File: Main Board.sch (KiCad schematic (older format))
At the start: 0 parts

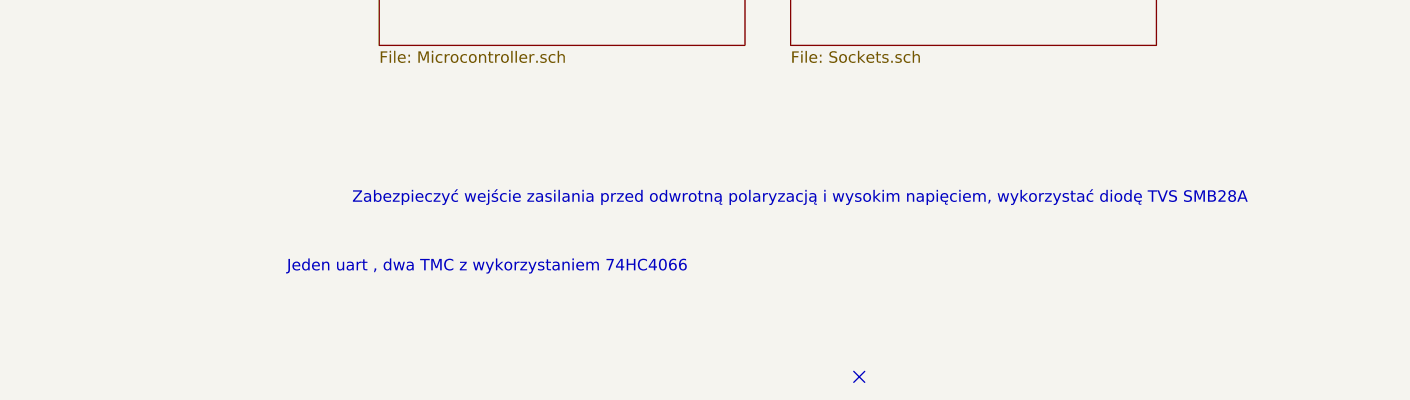
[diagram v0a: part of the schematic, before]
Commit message: Finished Power Managment
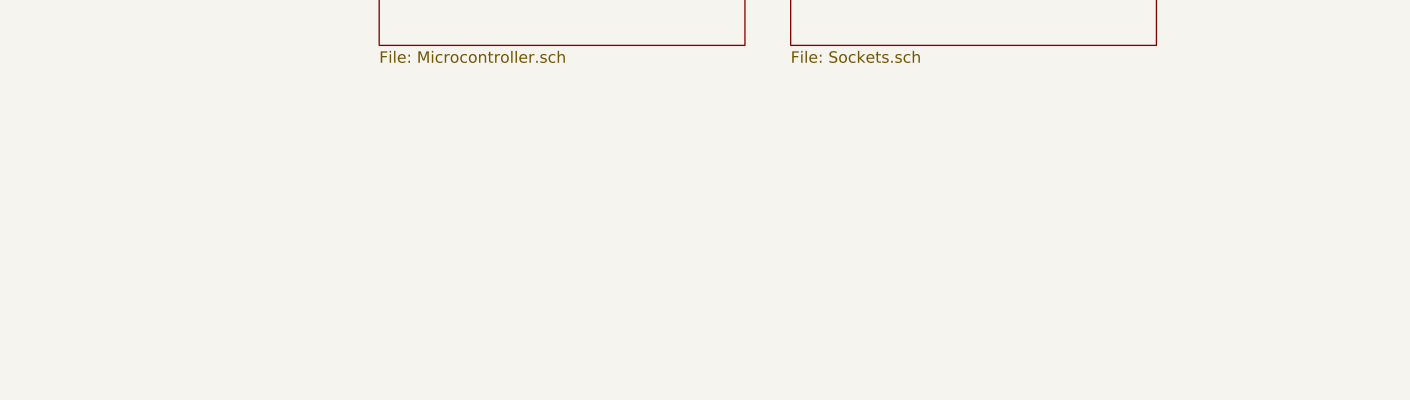
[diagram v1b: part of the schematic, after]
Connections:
- no-connect marks 1 -> 0
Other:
- note removed: "Jeden uart , dwa TMC z wykorzystaniem 74HC4066\n"
- note removed: "Zabezpieczyć wejście zasilania przed odwrotną polaryzacją i wysokim napięciem, wykorzystać diodę TVS SMB28A"
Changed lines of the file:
@@
 F1 "Sockets.sch" 50
 $EndSheet
-Text Notes 5550 3650 2    50   ~ 0
-Zabezpieczyć wejście zasilania przed odwrotną polaryzacją i wysokim napięciem, wykorzystać diodę TVS SMB28A
-NoConn ~ 3850 4400
-Text Notes 3100 3950 2    50   ~ 0
-Jeden uart , dwa TMC z wykorzystaniem 74HC4066\n
 $Sheet
 S 5400 800  1600 900

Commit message: Finished Emergency Circuit
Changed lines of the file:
@@
 $Descr A4 11693 8268
 encoding utf-8
-Sheet 1 6
+Sheet 1 9
 Title ""
 Date ""
@@
 F1 "Power.sch" 50
 $EndSheet
+$Sheet
+S 5400 2050 1600 900
+U 5E858220
+F0 "Sockets 2" 50
+F1 "Sockets 2.sch" 50
+$EndSheet
+$Sheet
+S 1750 3250 1600 900
+U 5E91D7CC
+F0 "Emergency" 50
+F1 "Emergency.sch" 50
+$EndSheet
+$Sheet
+S 3550 3250 1600 900
+U 5E91D96F
+F0 "HMI" 50
+F1 "HMI.sch" 50
+$EndSheet
 $EndSCHEMATC

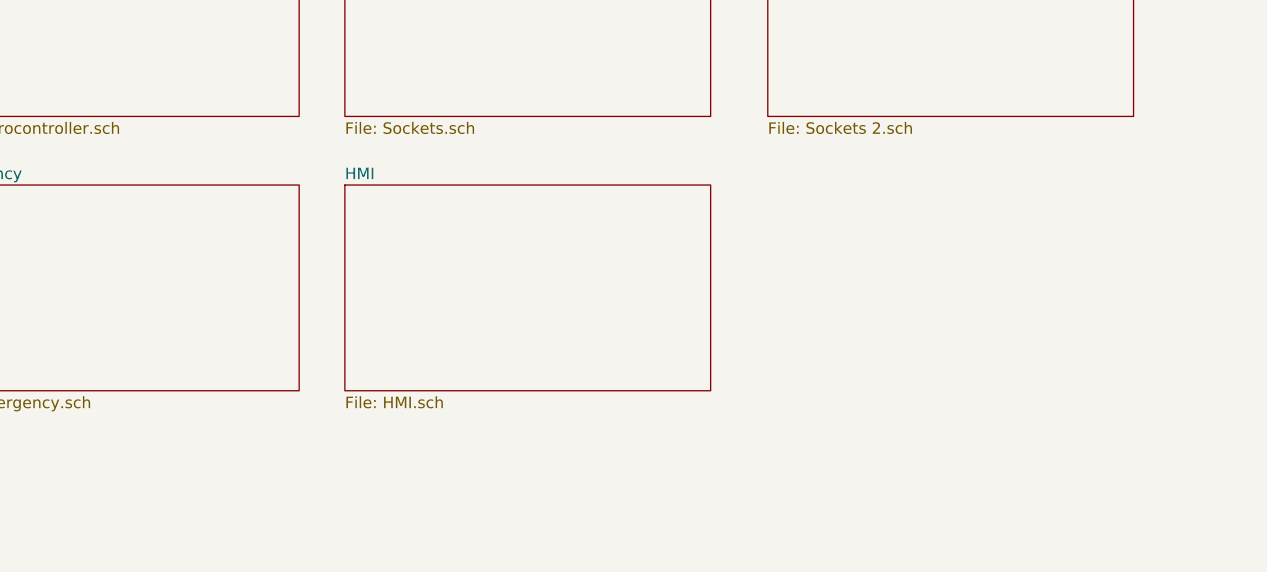
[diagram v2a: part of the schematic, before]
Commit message: Added Polyfuses and replace diodes
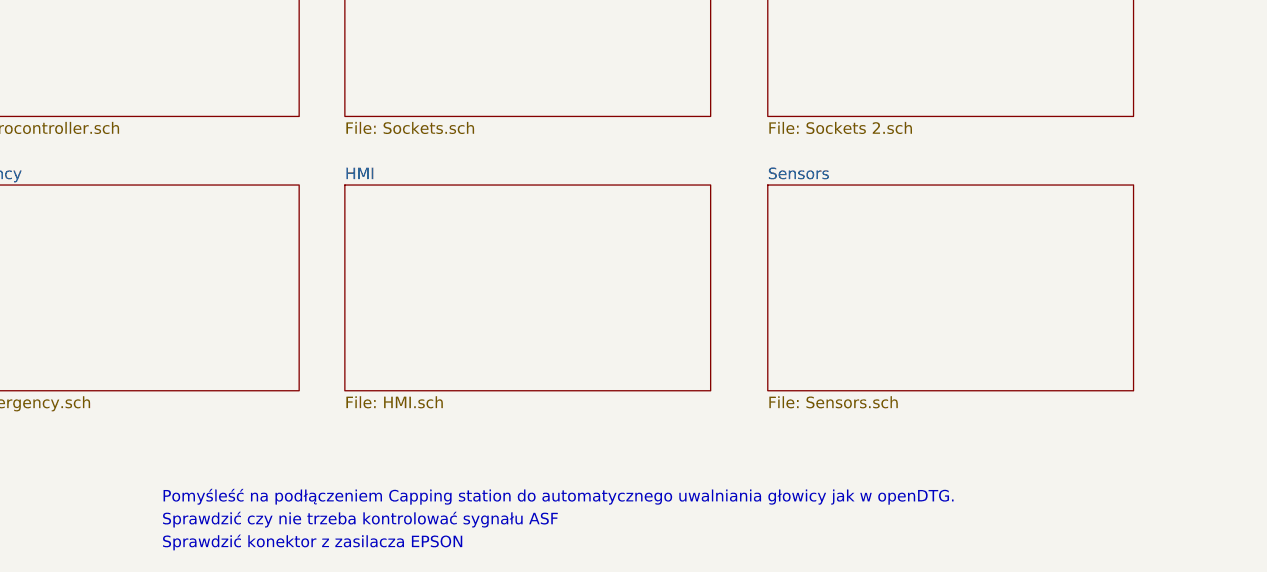
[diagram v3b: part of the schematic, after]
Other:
- note added: "Pomyśleść na podłączeniem Capping station do automatycznego uwalniania głowicy jak w openDTG."
- note added: "Sprawdzić czy nie trzeba kontrolować sygnału ASF"
- note added: "Sprawdzić konektor z zasilacza EPSON"
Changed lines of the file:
@@
 $Descr A4 11693 8268
 encoding utf-8
-Sheet 1 9
+Sheet 1 10
 Title ""
 Date ""
@@
 F1 "HMI.sch" 50
 $EndSheet
+$Sheet
+S 5400 3250 1600 900
+U 5E1B3A8F
+F0 "Sensors" 50
+F1 "Sensors.sch" 50
+$EndSheet
+Text Notes 2750 4650 0    50   ~ 0
+Pomyśleść na podłączeniem Capping station do automatycznego uwalniania głowicy jak w openDTG.
+Text Notes 2750 4750 0    50   ~ 0
+Sprawdzić czy nie trzeba kontrolować sygnału ASF
+Text Notes 2750 4850 0    50   ~ 0
+Sprawdzić konektor z zasilacza EPSON
 $EndSCHEMATC

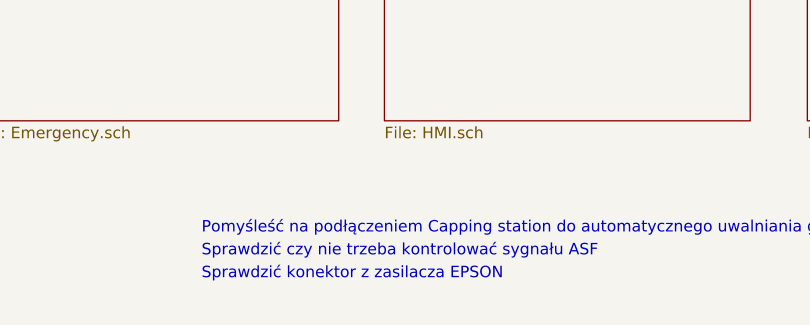
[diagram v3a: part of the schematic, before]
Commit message: Added USB B socket with ESD filter
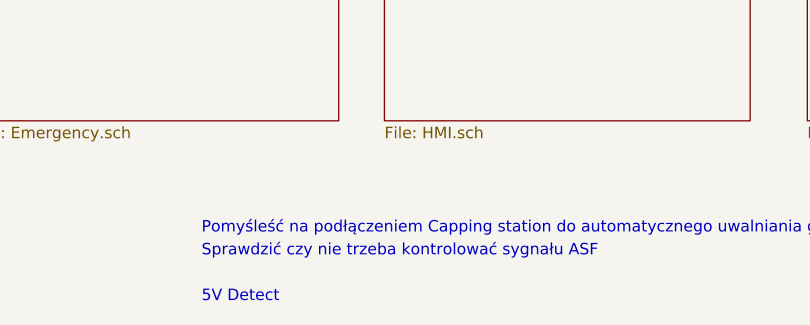
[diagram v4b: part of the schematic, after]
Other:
- note added: "5V Detect"
- note removed: "Sprawdzić konektor z zasilacza EPSON"
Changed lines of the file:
@@
 Text Notes 2750 4750 0    50   ~ 0
 Sprawdzić czy nie trzeba kontrolować sygnału ASF
-Text Notes 2750 4850 0    50   ~ 0
-Sprawdzić konektor z zasilacza EPSON
+Text Notes 2750 4950 0    50   ~ 0
+5V Detect
 $EndSCHEMATC

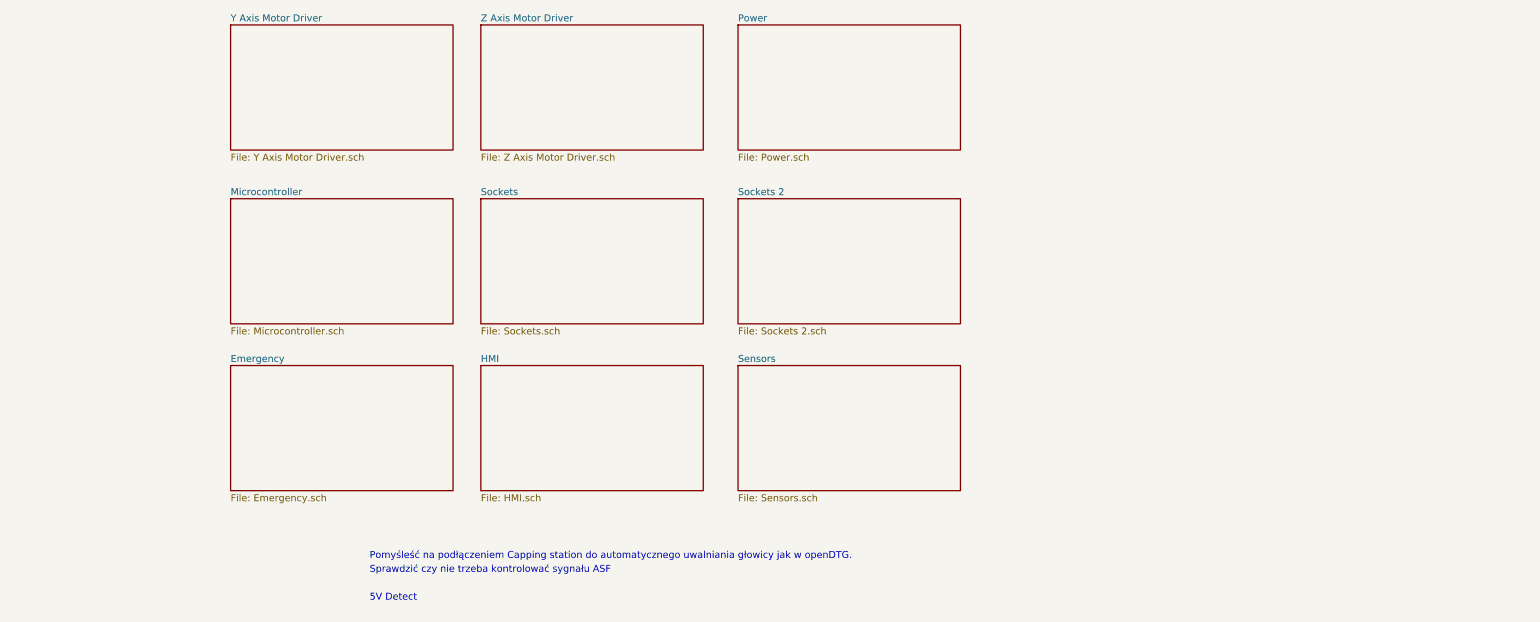
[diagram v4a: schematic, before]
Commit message: Numbering and finishing the schematic
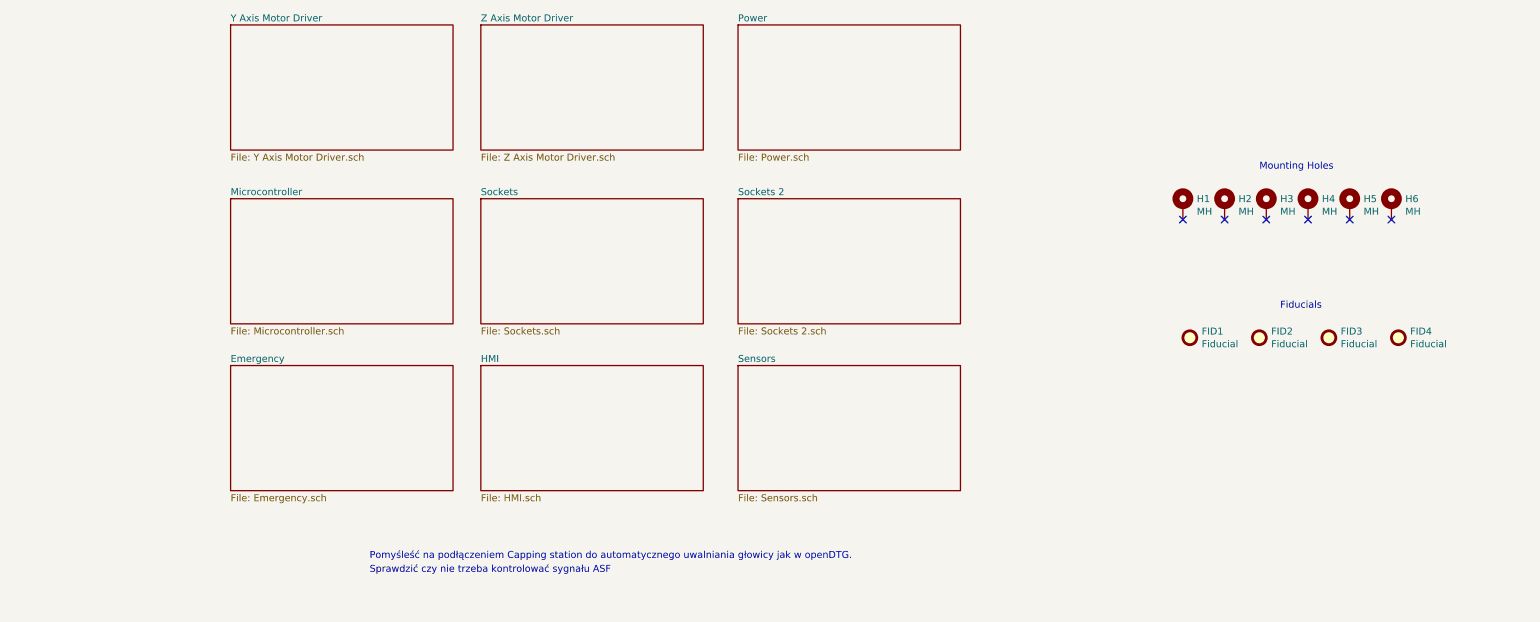
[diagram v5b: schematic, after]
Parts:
- added FID1, FID2, FID3, FID4: Fiducial, symbol Mechanical:Fiducial
- added H1, H2, H3, H4, H5, H6: MH, symbol Mechanical:MountingHole_Pad
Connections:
- no-connect marks 0 -> 6
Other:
- note added: "Fiducials"
- note added: "Mounting Holes"
- note removed: "5V Detect"
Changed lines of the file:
@@
 Text Notes 2750 4750 0    50   ~ 0
 Sprawdzić czy nie trzeba kontrolować sygnału ASF
-Text Notes 2750 4950 0    50   ~ 0
-5V Detect
+$Comp
+L Mechanical:MountingHole_Pad H1
+U 1 1 5E6920D8
+P 8600 2100
+F 0 "H1" H 8700 2149 50  0000 L CNN
+F 1 "MH" H 8700 2058 50  0000 L CNN
+F 2 "" H 8600 2100 50  0001 C CNN
+F 3 "~" H 8600 2100 50  0001 C CNN
+	1    8600 2100
+	1    0    0    -1
+$EndComp
+$Comp
+L Mechanical:MountingHole_Pad H2
+U 1 1 5E693034
+P 8900 2100
+F 0 "H2" H 9000 2149 50  0000 L CNN
+F 1 "MH" H 9000 2058 50  0000 L CNN
+F 2 "" H 8900 2100 50  0001 C CNN
+F 3 "~" H 8900 2100 50  0001 C CNN
+	1    8900 2100
+	1    0    0    -1
+$EndComp
+$Comp
+L Mechanical:MountingHole_Pad H3
+U 1 1 5E6931F2
+P 9200 2100
+F 0 "H3" H 9300 2149 50  0000 L CNN
+F 1 "MH" H 9300 2058 50  0000 L CNN
+F 2 "" H 9200 2100 50  0001 C CNN
+F 3 "~" H 9200 2100 50  0001 C CNN
+	1    9200 2100
+	1    0    0    -1
+$EndComp
+$Comp
+L Mechanical:MountingHole_Pad H4
+U 1 1 5E6933CD
+P 9500 2100
+F 0 "H4" H 9600 2149 50  0000 L CNN
+F 1 "MH" H 9600 2058 50  0000 L CNN
+F 2 "" H 9500 2100 50  0001 C CNN
+F 3 "~" H 9500 2100 50  0001 C CNN
+	1    9500 2100
+	1    0    0    -1
+$EndComp
+$Comp
+L Mechanical:MountingHole_Pad H5
+U 1 1 5E6935B4
+P 9800 2100
+F 0 "H5" H 9900 2149 50  0000 L CNN
+F 1 "MH" H 9900 2058 50  0000 L CNN
+F 2 "" H 9800 2100 50  0001 C CNN
+F 3 "~" H 9800 2100 50  0001 C CNN
+	1    9800 2100
+	1    0    0    -1
+$EndComp
+$Comp
+L Mechanical:MountingHole_Pad H6
+U 1 1 5E69378B
+P 10100 2100
+F 0 "H6" H 10200 2149 50  0000 L CNN
+F 1 "MH" H 10200 2058 50  0000 L CNN
+F 2 "" H 10100 2100 50  0001 C CNN
+F 3 "~" H 10100 2100 50  0001 C CNN
+	1    10100 2100
+	1    0    0    -1
+$EndComp
+NoConn ~ 8600 2200
+NoConn ~ 8900 2200
+NoConn ~ 9200 2200
+NoConn ~ 9500 2200
+NoConn ~ 9800 2200
+NoConn ~ 10100 2200
+$Comp
+L Mechanical:Fiducial FID1
+U 1 1 5E693F35
+P 8650 3050
+F 0 "FID1" H 8735 3096 50  0000 L CNN
+F 1 "Fiducial" H 8735 3005 50  0000 L CNN
+F 2 "" H 8650 3050 50  0001 C CNN
+F 3 "~" H 8650 3050 50  0001 C CNN
+	1    8650 3050
+	1    0    0    -1
+$EndComp
+$Comp
+L Mechanical:Fiducial FID2
+U 1 1 5E6942E3
+P 9150 3050
+F 0 "FID2" H 9235 3096 50  0000 L CNN
+F 1 "Fiducial" H 9235 3005 50  0000 L CNN
+F 2 "" H 9150 3050 50  0001 C CNN
+F 3 "~" H 9150 3050 50  0001 C CNN
+	1    9150 3050
+	1    0    0    -1
+$EndComp
+$Comp
+L Mechanical:Fiducial FID3
+U 1 1 5E694478
+P 9650 3050
+F 0 "FID3" H 9735 3096 50  0000 L CNN
+F 1 "Fiducial" H 9735 3005 50  0000 L CNN
+F 2 "" H 9650 3050 50  0001 C CNN
+F 3 "~" H 9650 3050 50  0001 C CNN
+	1    9650 3050
+	1    0    0    -1
+$EndComp
+$Comp
+L Mechanical:Fiducial FID4
+U 1 1 5E694686
+P 10150 3050
+F 0 "FID4" H 10235 3096 50  0000 L CNN
+F 1 "Fiducial" H 10235 3005 50  0000 L CNN
+F 2 "" H 10150 3050 50  0001 C CNN
+F 3 "~" H 10150 3050 50  0001 C CNN
+	1    10150 3050
+	1    0    0    -1
+$EndComp
+Text Notes 9150 1850 0    50   ~ 0
+Mounting Holes
+Text Notes 9300 2850 0    50   ~ 0
+Fiducials
 $EndSCHEMATC

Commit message: Shematic almost finished, BOM in KiCad 3/4 finished
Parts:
- FID1, FID2, FID3, FID4: footprint (none) -> Fiducial:Fiducial_1mm_Mask2mm
- H1, H2, H3, H4, H5, H6: footprint (none) -> MountingHole:MountingHole_3.5mm_Pad_Via
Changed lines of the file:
@@
 F 0 "H1" H 8700 2149 50  0000 L CNN
 F 1 "MH" H 8700 2058 50  0000 L CNN
-F 2 "" H 8600 2100 50  0001 C CNN
+F 2 "MountingHole:MountingHole_3.5mm_Pad_Via" H 8600 2100 50  0001 C CNN
 F 3 "~" H 8600 2100 50  0001 C CNN
 	1    8600 2100
@@
 F 0 "H2" H 9000 2149 50  0000 L CNN
 F 1 "MH" H 9000 2058 50  0000 L CNN
-F 2 "" H 8900 2100 50  0001 C CNN
+F 2 "MountingHole:MountingHole_3.5mm_Pad_Via" H 8900 2100 50  0001 C CNN
 F 3 "~" H 8900 2100 50  0001 C CNN
 	1    8900 2100
@@
 F 0 "H3" H 9300 2149 50  0000 L CNN
 F 1 "MH" H 9300 2058 50  0000 L CNN
-F 2 "" H 9200 2100 50  0001 C CNN
+F 2 "MountingHole:MountingHole_3.5mm_Pad_Via" H 9200 2100 50  0001 C CNN
 F 3 "~" H 9200 2100 50  0001 C CNN
 	1    9200 2100
@@
 F 0 "H4" H 9600 2149 50  0000 L CNN
 F 1 "MH" H 9600 2058 50  0000 L CNN
-F 2 "" H 9500 2100 50  0001 C CNN
+F 2 "MountingHole:MountingHole_3.5mm_Pad_Via" H 9500 2100 50  0001 C CNN
 F 3 "~" H 9500 2100 50  0001 C CNN
 	1    9500 2100
@@
 F 0 "H5" H 9900 2149 50  0000 L CNN
 F 1 "MH" H 9900 2058 50  0000 L CNN
-F 2 "" H 9800 2100 50  0001 C CNN
+F 2 "MountingHole:MountingHole_3.5mm_Pad_Via" H 9800 2100 50  0001 C CNN
 F 3 "~" H 9800 2100 50  0001 C CNN
 	1    9800 2100
@@
 F 0 "H6" H 10200 2149 50  0000 L CNN
 F 1 "MH" H 10200 2058 50  0000 L CNN
-F 2 "" H 10100 2100 50  0001 C CNN
+F 2 "MountingHole:MountingHole_3.5mm_Pad_Via" H 10100 2100 50  0001 C CNN
 F 3 "~" H 10100 2100 50  0001 C CNN
 	1    10100 2100
@@
 F 0 "FID1" H 8735 3096 50  0000 L CNN
 F 1 "Fiducial" H 8735 3005 50  0000 L CNN
-F 2 "" H 8650 3050 50  0001 C CNN
+F 2 "Fiducial:Fiducial_1mm_Mask2mm" H 8650 3050 50  0001 C CNN
 F 3 "~" H 8650 3050 50  0001 C CNN
 	1    8650 3050
@@
 F 0 "FID2" H 9235 3096 50  0000 L CNN
 F 1 "Fiducial" H 9235 3005 50  0000 L CNN
-F 2 "" H 9150 3050 50  0001 C CNN
+F 2 "Fiducial:Fiducial_1mm_Mask2mm" H 9150 3050 50  0001 C CNN
 F 3 "~" H 9150 3050 50  0001 C CNN
 	1    9150 3050
@@
 F 0 "FID3" H 9735 3096 50  0000 L CNN
 F 1 "Fiducial" H 9735 3005 50  0000 L CNN
-F 2 "" H 9650 3050 50  0001 C CNN
+F 2 "Fiducial:Fiducial_1mm_Mask2mm" H 9650 3050 50  0001 C CNN
 F 3 "~" H 9650 3050 50  0001 C CNN
 	1    9650 3050
@@
 F 0 "FID4" H 10235 3096 50  0000 L CNN
 F 1 "Fiducial" H 10235 3005 50  0000 L CNN
-F 2 "" H 10150 3050 50  0001 C CNN
+F 2 "Fiducial:Fiducial_1mm_Mask2mm" H 10150 3050 50  0001 C CNN
 F 3 "~" H 10150 3050 50  0001 C CNN
 	1    10150 3050

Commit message: Generated BOM
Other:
- note added: "Generowanie BOM:\nxsltproc -o "X:/DTG/PCB/P600-Main-Board/GrupedBOMRaw.csv" "C:\Program Files\KiCad\bin\scripting\plugins\bom2grouped_csv.xsl" "X:\DTG\PCB\P600-Main-Board\Main Board.xml""
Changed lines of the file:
@@
 Text Notes 9300 2850 0    50   ~ 0
 Fiducials
+Text Notes 2750 5000 0    50   ~ 0
+Generowanie BOM:\nxsltproc -o "X:/DTG/PCB/P600-Main-Board/GrupedBOMRaw.csv" "C:\Program Files\KiCad\bin\scripting\plugins\bom2grouped_csv.xsl" "X:\DTG\PCB\P600-Main-Board\Main Board.xml"
 $EndSCHEMATC

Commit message: Rozmieszczenie elementów, trasowanie ścieżek, etap 2/4
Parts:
- added FID5, FID6: Fiducial, Fiducial:Fiducial_1mm_Mask2mm, symbol Mechanical:Fiducial
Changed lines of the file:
@@
 Text Notes 2750 5000 0    50   ~ 0
 Generowanie BOM:\nxsltproc -o "X:/DTG/PCB/P600-Main-Board/GrupedBOMRaw.csv" "C:\Program Files\KiCad\bin\scripting\plugins\bom2grouped_csv.xsl" "X:\DTG\PCB\P600-Main-Board\Main Board.xml"
+$Comp
+L Mechanical:Fiducial FID5
+U 1 1 5E310D94
+P 8650 3300
+F 0 "FID5" H 8735 3346 50  0000 L CNN
+F 1 "Fiducial" H 8735 3255 50  0000 L CNN
+F 2 "Fiducial:Fiducial_1mm_Mask2mm" H 8650 3300 50  0001 C CNN
+F 3 "~" H 8650 3300 50  0001 C CNN
+	1    8650 3300
+	1    0    0    -1
+$EndComp
+$Comp
+L Mechanical:Fiducial FID6
+U 1 1 5E3112BF
+P 9150 3300
+F 0 "FID6" H 9235 3346 50  0000 L CNN
+F 1 "Fiducial" H 9235 3255 50  0000 L CNN
+F 2 "Fiducial:Fiducial_1mm_Mask2mm" H 9150 3300 50  0001 C CNN
+F 3 "~" H 9150 3300 50  0001 C CNN
+	1    9150 3300
+	1    0    0    -1
+$EndComp
 $EndSCHEMATC
